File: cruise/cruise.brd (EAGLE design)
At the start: 75.2 x 80 mm, 87 parts, among them IC1 24C04ASM, IC3 LD117AS33TR, Q1 BSS138, Q2 BSS138, Q3 BSS138, Q4 8MHz, U1 STM32F103CBT6, X2 JST-XH-04-PIN-LONG-PAD, X5 SWD, X6 I2C, X7 JST-XH-06-PIN-LONG-PAD

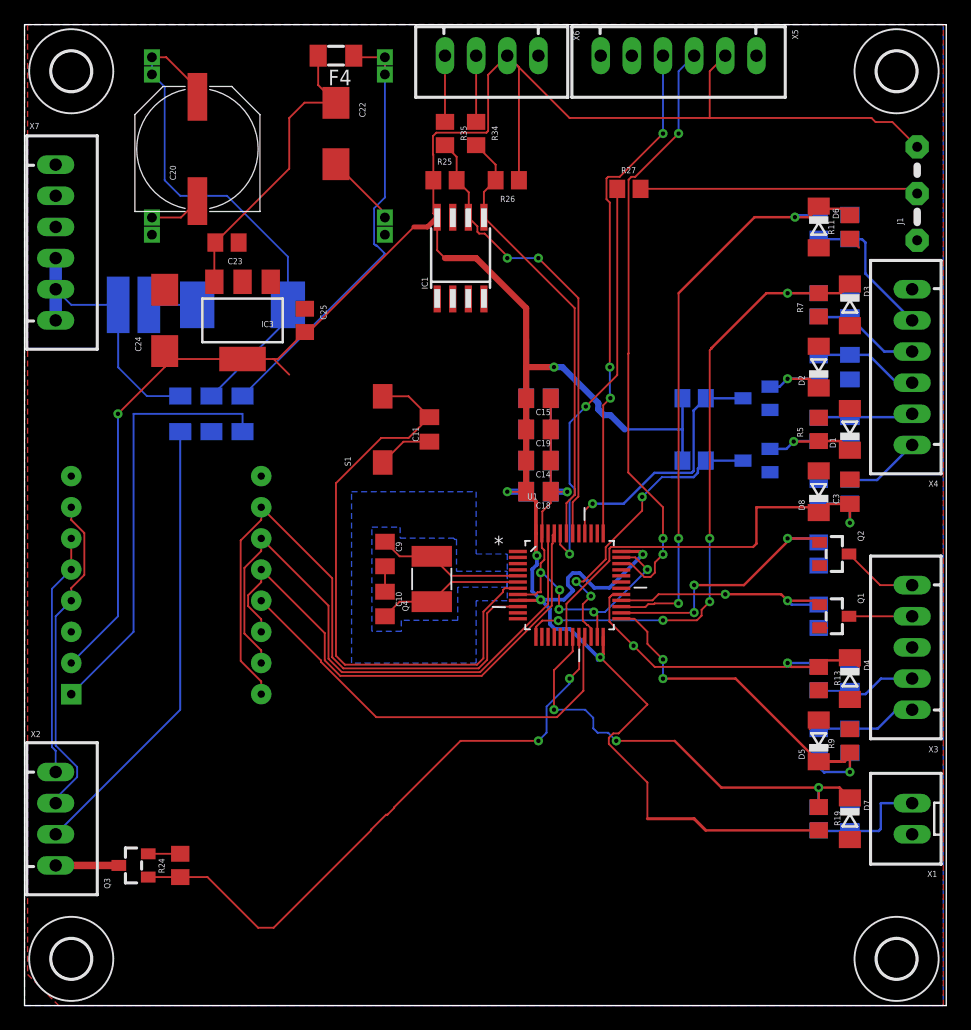
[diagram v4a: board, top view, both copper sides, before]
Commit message: PWM+PID
Заработал нормально Pwm 20khz
Заработал вменяемо PID
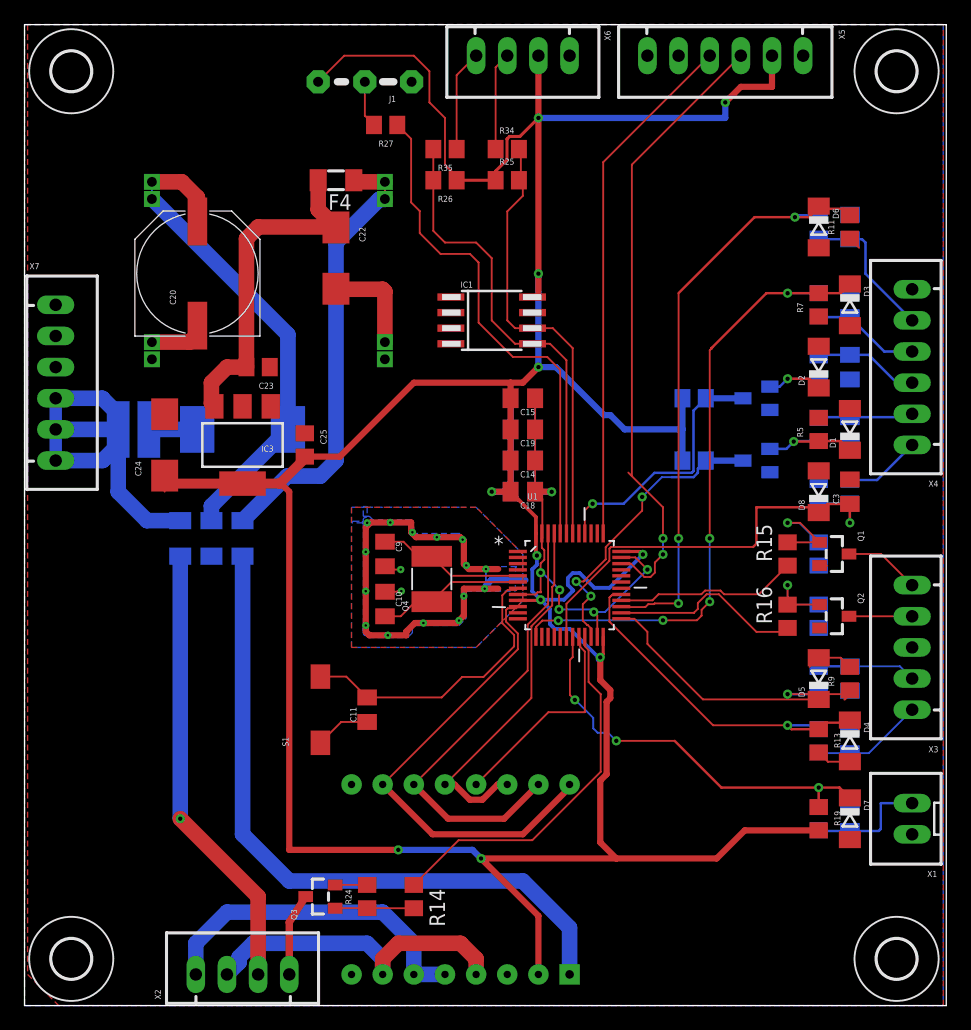
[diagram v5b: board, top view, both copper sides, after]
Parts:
- added R14, R15, R16: 200, resistor:R0805
- Q1, Q2, Q3: value BSS138 -> AO4300
- moved J1 44.5 mm to (30.9, 75.3), turned to 180 degrees
- moved TB1 34.3 mm to (39.4, 10.2), turned to 90 degrees
- moved C11 23.4 mm to (29.2, 24.1)
- moved S1 23.4 mm to (25.4, 24.1)
- moved R27 20.5 mm to (30.7, 71.8), turned to 180 degrees
- moved X2 19.8 mm to (19.1, 2.54), turned to 0 degrees
- moved R24 15.5 mm to (29.2, 8.89)
- moved Q3 15.5 mm to (25.4, 8.89)
- moved X7 11.4 mm to (3.81, 50.8)
- moved C23 10.5 mm to (20.3, 52.1)
- moved C22 10.2 mm to (26.7, 61.0)
- moved C24 10.2 mm to (12.7, 45.7)
- moved C25 10.2 mm to (24.1, 45.7)
- moved IC3 10.2 mm to (19.1, 45.7)
- moved C20 10.2 mm to (15.4, 59.7)
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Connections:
- net N$18 renamed PB5_OUT_SOLENOID
- removed net N$20: U1.39
- removed net PB2_OUT_SOLENOID: Q3.1, R24.1, U1.20
- removed net VNH2_SP30_EN: TB1.STBY, U1.21
- new net N$10: Q1.1, R15.2, R22.1
- new net N$14: Q2.1, R16.2, R23.1
- new net N$8: Q3.1, R14.2, R24.1
- new net PB10_OUT_SOLENOID: R14.1, U1.21
- new net TB6612FNG_STB: TB1.STBY, U1.20
- net CRUISE_LAMP_OUT_PB15: now also R15.1; no longer Q1.1, R22.1
- net D_IN: now also X3.1; no longer X3.2
- net N$32: now also X3.5; no longer X3.4
- net N$35: now also X3.4; no longer X3.5
- net OD_IN_L: now also X3.2; no longer X3.1
- net OD_OUT_BUTTON_PB13: now also R16.1; no longer Q2.1, R23.1
- net SCL: now also R34.2; no longer R35.2
- net SDA: now also R35.2; no longer R34.2
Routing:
- net GND: track 65.5 -> 117.1 mm, vias 6 -> 23
- net PB2_OUT_SOLENOID: track 49.8 -> 0.00 mm, vias 2 -> 0
- net VCC: track 267.5 -> 305.7 mm, vias 7 -> 11
- net VNH2_SP30_EN: track 35.6 -> 0.00 mm
- net PB10_OUT_SOLENOID: track 0.00 -> 30.6 mm
- net RST: track 48.5 -> 24.3 mm
- net +12V2A_MOTOR: track 35.3 -> 56.3 mm
- net N$7: track 22.7 -> 3.83 mm
- net TB6612FNG_STB: track 0.00 -> 17.7 mm
- net +12V: track 21.8 -> 38.9 mm
- net VNH2_SP30_INA: track 42.9 -> 30.3 mm
- net VNH2_SP30_INB: track 49.8 -> 37.5 mm
- net VNH2_SP30_PWM: track 51.1 -> 39.0 mm
- net N$10: track 0.00 -> 9.08 mm, vias 0 -> 1
- net N$14: track 0.00 -> 8.14 mm, vias 0 -> 1
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- added copper zone on layer 16, net OCS_CUTOUT
- added copper zone on layer 1, net OSC_CUTOUT
- added copper zone on layer 16, net OSC_GND_REMOVE
- removed copper zone on layer 16, net NC

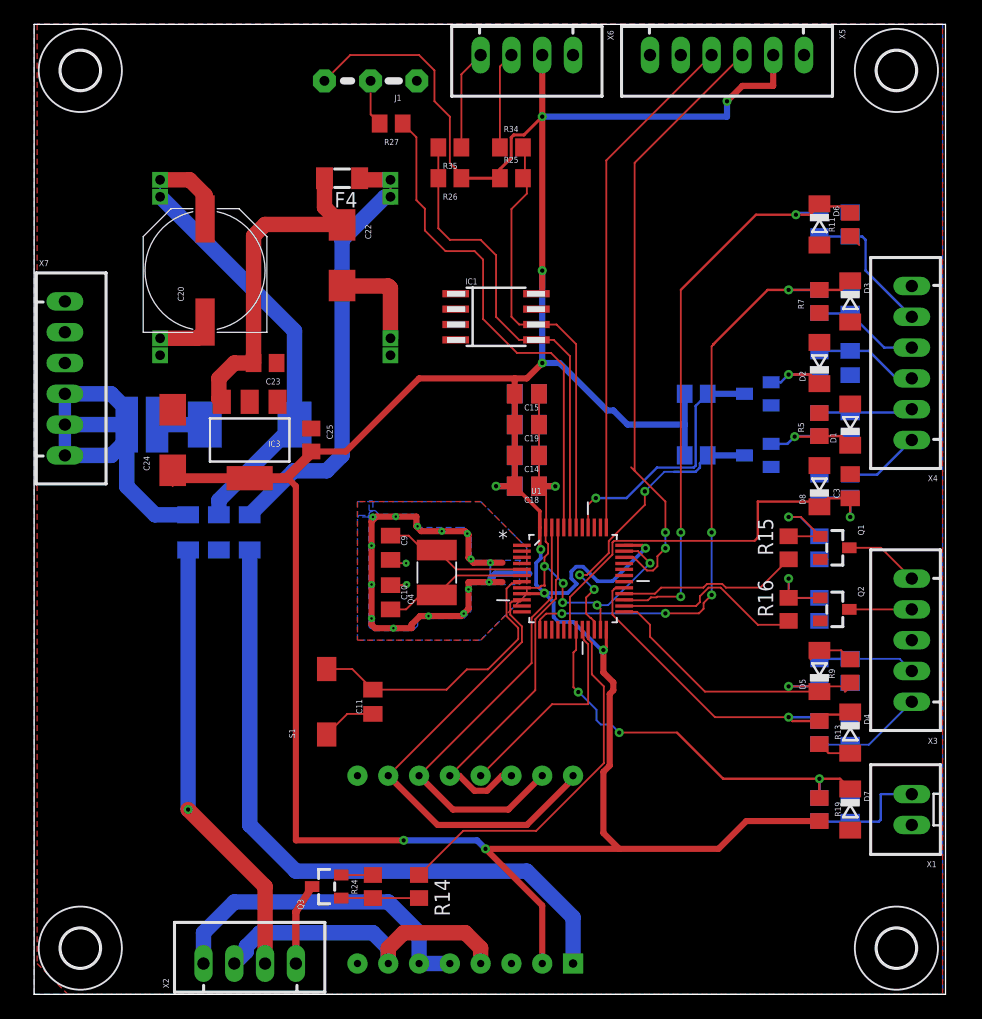
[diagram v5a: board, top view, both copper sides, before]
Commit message: добавлен функционал тюна пидов
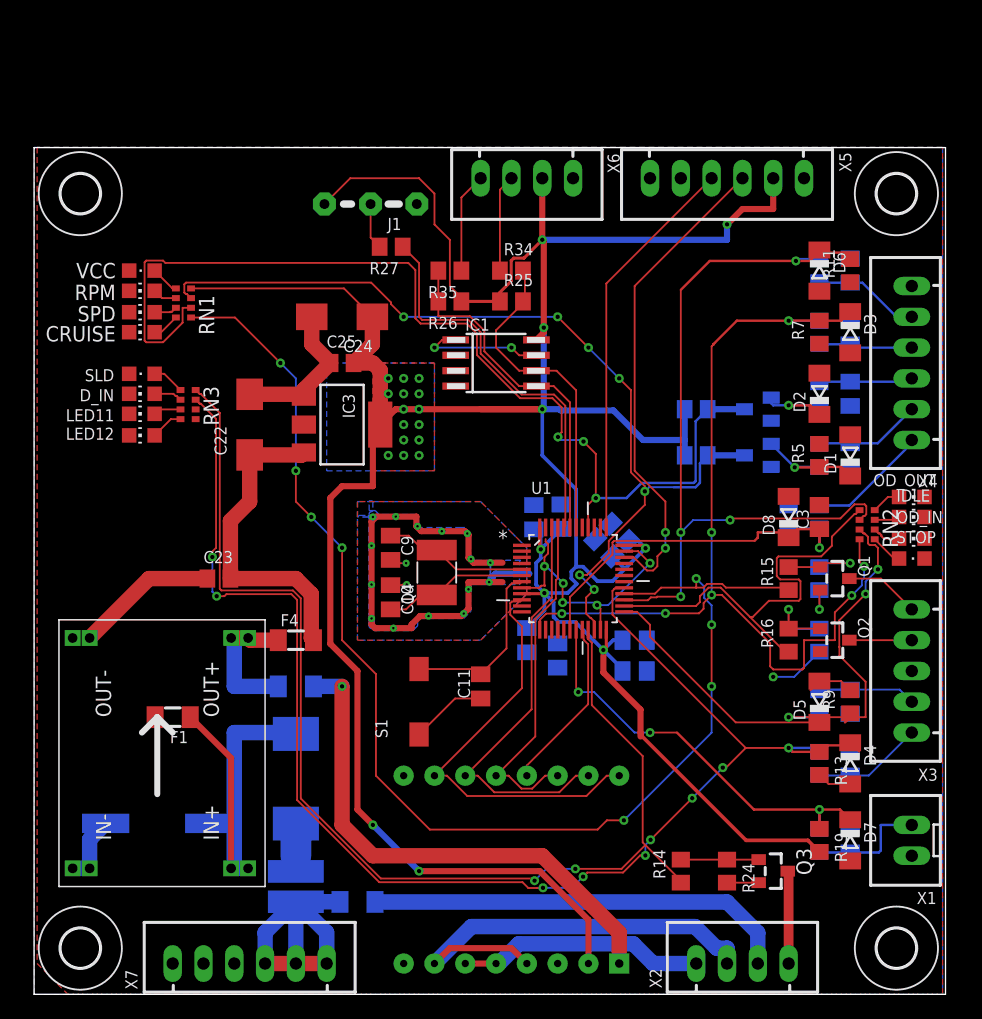
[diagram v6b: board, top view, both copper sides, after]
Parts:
- added CRUISE, D_IN, IDLE, LED11, LED12, OD_IN, OD_OUT, RPM, SPD: (no value), led:CHIP-LED0805
- added RN1, RN2, RN3: (no value), resistor-dil:0603-ARV
- added SLD, STOP, VCC: (no value), led:CHIPLED_0805
- moved U$6 60.5 mm to (20.3, 8.89), flipped to the top, turned to 90 degrees
- moved X7 50.6 mm to (19.1, 2.54), turned to 0 degrees
- moved C20 45.8 mm to (11.4, 14.1), flipped to the bottom, turned to 180 degrees
- moved X2 40.6 mm to (59.7, 2.54)
- moved U$1 40.2 mm to (22.9, 8.89), turned to 90 degrees
- moved F4 38.3 mm to (22.9, 29.2), turned to 0 degrees
- moved Q3 36.9 mm to (62.2, 10.2), turned to 270 degrees
- moved F2 33.5 mm to (27.9, 7.62), turned to 180 degrees
- moved D9 29.5 mm to (22.9, 17.8), turned to 270 degrees
- moved R24 29.2 mm to (58.4, 10.2), turned to 270 degrees
- moved R14 21.6 mm to (54.6, 10.2), turned to 90 degrees
- moved C12 20.3 mm to (41.9, 29.2), turned to 90 degrees
- moved C14 19.9 mm to (50.8, 26.7), flipped to the bottom, turned to 0 degrees
- moved C16 19.9 mm to (50.8, 29.2)
- moved C19 19.2 mm to (44.5, 27.9), flipped to the bottom, turned to 90 degrees
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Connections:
- new net N$15: RN1.2, RPM.A
- new net N$16: RN1.1, VCC.A
- new net N$17: RN1.3, SPD.A
- new net N$18: CRUISE.A, RN1.4
- new net N$19: RN2.1, STOP.A
- new net N$20: OD_IN.A, RN2.2
- new net N$21: IDLE.A, RN2.3
- new net N$23: OD_OUT.A, RN2.4
- new net N$24: RN3.1, SLD.A
- new net N$27: D_IN.A, RN3.2
- new net N$31: LED11.A, RN3.3
- new net N$33: LED12.A, RN3.4
- net CRUISE_LAMP_OUT_PB15: now also RN1.5
- net D_IN_PA8: now also RN3.7
- net GND: now also CRUISE.C, D_IN.C, IDLE.C, LED11.C, LED12.C, OD_IN.C, OD_OUT.C, RPM.C, SLD.C, SPD.C, STOP.C, VCC.C
- net IDLE_IN_PB14: now also RN2.6
- net OD_IN_LIGHT_PB12: now also RN2.7
- net OD_OUT_BUTTON_PB13: now also RN2.5
- net PB10_OUT_SOLENOID: now also RN3.8
- net RPM_EXTI11: now also RN1.7
- net STOP_IN_PA3: now also RN2.8
- net TIM3_CH2_SPD: now also RN1.6
- net VCC: now also RN1.8
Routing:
- net CRUISE_LAMP_OUT_PB15: track 15.0 -> 107.1 mm, vias 0 -> 8
- net D_IN_PA8: track 30.4 -> 117.4 mm, vias 1 -> 9
- net PB10_OUT_SOLENOID: track 30.6 -> 97.3 mm, vias 0 -> 2
- net TIM3_CH2_SPD: track 21.5 -> 85.9 mm, vias 1 -> 3
- net RPM_EXTI11: track 24.7 -> 76.4 mm, vias 3 -> 7
- net N$5: track 38.3 -> 11.7 mm
- net STOP_IN_PA3: track 53.1 -> 77.7 mm, vias 5 -> 7
- net OD_IN_LIGHT_PB12: track 28.6 -> 49.6 mm, vias 1 -> 3
- net OD_OUT_BUTTON_PB13: track 15.9 -> 35.6 mm
- net IDLE_IN_PB14: track 50.6 -> 66.7 mm, vias 3 -> 4
- net VCC: track 305.7 -> 289.9 mm, vias 11 -> 25
- net +12V2A_MOTOR: track 56.3 -> 42.9 mm, vias 0 -> 1
- net +12V: track 38.9 -> 26.1 mm
- net GND: track 117.1 -> 128.5 mm, vias 23 -> 26
- net SWDIO: track 50.9 -> 40.3 mm
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- added copper zone on layer 1, net VCC
- added copper zone on layer 16, net VCC
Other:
- board size 75.2 x 80 mm -> 75.2 x 69.8 mm

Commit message: измененние схемы
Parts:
- removed CRUISE, D_IN, IDLE, LED11, LED12, OD_IN, OD_OUT, RPM, SPD: (no value), led:CHIP-LED0805
- removed R3: 4.7K, resistor:R0805
- removed RN1, RN2, RN3: (no value), resistor-dil:0603-ARV
- removed SLD, STOP, VCC: (no value), led:CHIPLED_0805
- removed T1, T2: (no value), transistor-neu-to92:SOT23-BEC
- MOT: value JST-XH-04-PIN-LONG-PAD -> (none)
- PWR: value JST-XH-06-PIN-LONG-PAD -> (none)
- R11, R13, R7, R9: value 3.3K -> 3K
- moved R4 84.1 mm to (3.81, -21.6), flipped to the top
- renumbered X1 to SW, X2 to MOT, X3 to IO1, X7 to PWR
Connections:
- removed net N$15: RN1.2, RPM.A
- removed net N$16: RN1.1, VCC.A
- removed net N$17: RN1.3, SPD.A
- removed net N$18: CRUISE.A, RN1.4
- removed net N$19: RN2.1, STOP.A
- removed net N$20: OD_IN.A, RN2.2
- removed net N$21: IDLE.A, RN2.3
- removed net N$23: OD_OUT.A, RN2.4
- removed net N$24: RN3.1, SLD.A
- removed net N$27: D_IN.A, RN3.2
- removed net N$31: LED11.A, RN3.3
- removed net N$33: LED12.A, RN3.4
- removed net N$4: D1.C, R2.2, R5.1, T2.B
- removed net N$6: D2.C, R1.2, T1.B
- net CRUISE_LAMP_OUT_PB15: no longer RN1.5
- net D_IN_PA8: no longer RN3.7
- net GND: now also R4.2; no longer CRUISE.C, D_IN.C, IDLE.C, LED11.C, LED12.C, OD_IN.C, OD_OUT.C, RPM.C, SLD.C, SPD.C, STOP.C, T1.E, T2.E, VCC.C
- net IDLE_IN_PB14: no longer RN2.6
- net OD_IN_LIGHT_PB12: no longer RN2.7
- net OD_OUT_BUTTON_PB13: no longer RN2.5
- net PB10_OUT_SOLENOID: no longer RN3.8
- net RPM_EXTI11: now also D1.C, R2.2, R5.1; no longer R4.1, RN1.7, T2.C
- net STOP_IN_PA3: no longer RN2.8
- net TIM3_CH2_SPD: now also D2.C, R1.2, R4.1; no longer R3.1, RN1.6, T1.C
- net VCC: no longer R3.2, R4.2, RN1.8
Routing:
- net VCC: track 289.9 -> 273.5 mm
- net N$4: track 9.71 -> 0.00 mm, vias 1 -> 0
- net N$6: track 7.36 -> 0.00 mm, vias 1 -> 0
- net CRUISE_LAMP_OUT_PB15: track 107.1 -> 103.5 mm
- net N$33: track 2.69 -> 0.00 mm
- net N$24: track 2.69 -> 0.00 mm
- net N$19: track 2.67 -> 0.00 mm
- net RPM_EXTI11: track 76.4 -> 78.9 mm, vias 7 -> 8
- net N$23: track 2.46 -> 0.00 mm
- net N$20: track 2.37 -> 0.00 mm
- net N$16: track 2.36 -> 0.00 mm
- net N$27: track 2.34 -> 0.00 mm
- net N$31: track 2.28 -> 0.00 mm
- net N$18: track 2.26 -> 0.00 mm
- net N$21: track 2.11 -> 0.00 mm
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
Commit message: работа со схемой
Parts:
- removed F1: 500mA, m-pad-2.1:1206
- removed X4: (no value), Rembrandt Electronics - JST XH Connectors v1-0:JST-XH-06-PACKAGE-LONG-PAD
- added C21: 470uF, rcl:PANASONIC_G
- added CTS, PA15_ADC, PC13, RTC-14, RTC-15, RTS: TPTP09R, testpad:TP09R
- added IO2: (no value), Rembrandt Electronics - JST XH Connectors v1-0:JST-XH-06-PACKAGE-LONG-PAD
- added PA1_ADC, PA2_ADC, PA4_ADC, PA5_ADC, PA6_ADC, PA7_ADC, PB3, PB5: (no value), testpad:TP09R
- IO1: device Rembrandt Electronics - JST XH Connectors v1-0:JST-XH-05-PACKAGE-LONG-PAD -> Rembrandt Electronics - JST XH Connectors v1-0:JST-XH-04-PACKAGE-LONG-PAD
- moved R4 89.8 mm to (68.6, 40.6), turned to 90 degrees
- moved R35 14.8 mm to (27.9, 47.0), turned to 270 degrees
- moved C25 14.5 mm to (13.6, 45.7)
- moved IC3 14.5 mm to (13.6, 40.6)
- moved C22 14.5 mm to (5.97, 40.6)
- moved C24 14.4 mm to (14.0, 49.1)
- moved R26 14.4 mm to (25.4, 47.0), turned to 270 degrees
- moved J1 14.1 mm to (23.2, 53.4)
- moved R27 13.7 mm to (23.1, 50.2)
- moved X6 13.7 mm to (34.3, 55.9)
- moved C6 13.7 mm to (68.5, 46.0)
- moved D6 13.7 mm to (65.9, 46.0)
- moved R10 13.7 mm to (65.9, 46.0)
- moved R11 13.7 mm to (68.5, 46.0)
- moved R6 13.0 mm to (60.1, 43.1)
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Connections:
- removed net 12V_500MA_SENSORS: F1.2
- removed net N$22: C20.+, D9.C, F1.1, U$6.IN1+, U$6.IN2+
- removed net N$34: U1.30
- removed net N$36: U1.31
- removed net N$41: U1.38
- removed net PB5_OUT_SOLENOID: U1.41
- new net N$15: PC13.TP, U1.2
- new net N$16: RTC-14.TP, U1.3
- new net N$17: RTC-15.TP, U1.4
- new net N$18: C20.+, D9.C, U$6.IN1+, U$6.IN2+
- new net N$4: PA7_ADC.TP, U1.17
- new net N$6: PB3.TP, U1.39
- new net PA15_ADC: PA15_ADC.TP, U1.38
- new net PB5: PB5.TP, U1.41
- new net RX: U1.31, X5.5
- new net TX: U1.30, X5.6
- net GND: now also C21.-; no longer X4.6
- net IDLE_IN: now also IO2.5; no longer X4.5
- net N$25: now also PA1_ADC.TP
- net N$26: now also PA2_ADC.TP
- net N$28: now also PA4_ADC.TP
- net N$29: now also PA6_ADC.TP
- net N$30: now also PA5_ADC.TP
- net N$32: now also IO1.4; no longer IO1.5
- net N$35: now also IO1.3; no longer IO1.4
- net N$37: now also CTS.TP
- net N$38: now also RTS.TP
- net N$5: now also C21.+
- net RPM_IN: now also IO2.2; no longer X4.2
- net SPD_IN: now also IO2.3; no longer X4.3
- net STOP_IN: now also IO2.4; no longer X4.4
- net TPS_IN: now also IO2.1; no longer X4.1
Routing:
- net CRUISE_LAMP_OUT_PB15: track 103.5 -> 13.4 mm, vias 8 -> 0
- net D_IN_PA8: track 117.0 -> 33.8 mm, vias 9 -> 1
- net PB10_OUT_SOLENOID: track 96.8 -> 24.0 mm, vias 2 -> 0
- net TIM3_CH2_SPD: track 87.7 -> 34.4 mm, vias 4 -> 3
- net RPM_EXTI11: track 78.9 -> 33.4 mm, vias 8 -> 3
- net N$18: track 0.00 -> 36.1 mm
- net N$22: track 33.7 -> 0.00 mm
- net VCC: track 273.5 -> 241.5 mm, vias 25 -> 27
- net IDLE_IN_PB14: track 66.3 -> 35.4 mm, vias 4 -> 3
- net STOP_IN_PA3: track 75.8 -> 45.7 mm
- net RX: track 0.00 -> 27.3 mm, vias 0 -> 3
- net TX: track 0.00 -> 26.1 mm, vias 0 -> 3
- net OD_OUT_BUTTON_PB13: track 35.1 -> 15.0 mm
- net OD_IN_LIGHT_PB12: track 49.1 -> 31.8 mm, vias 3 -> 1
- net PA15_ADC: track 0.00 -> 11.8 mm
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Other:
- board size 75.2 x 69.8 mm -> 75.2 x 58.4 mm
